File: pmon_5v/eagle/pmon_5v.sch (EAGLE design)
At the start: 33 parts, among them J1 USB, J2 USB, J3 USB_A, J4 PINHD-2X3, Q1 16Mhz, U1 LTC2943, U2 FT232RL, U3 ATMEGA328TQFP32, U4 TC1015

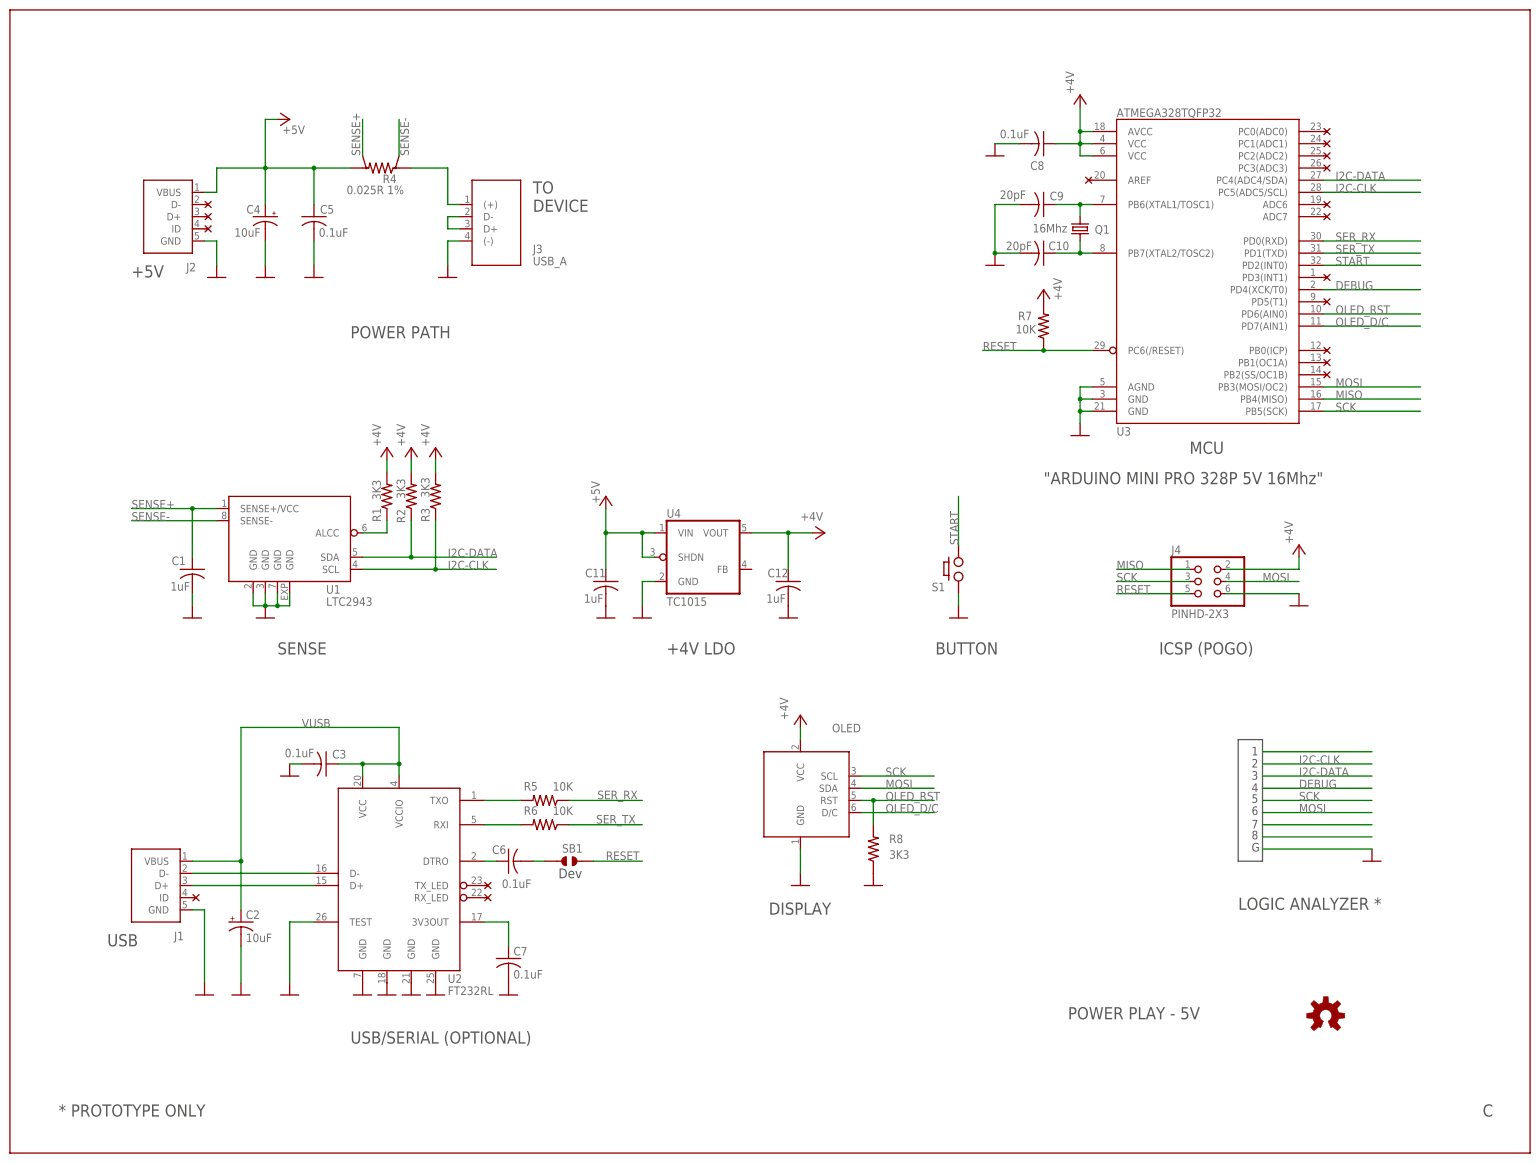
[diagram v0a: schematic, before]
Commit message: Renamed +4V network to VCC. No semantic change.
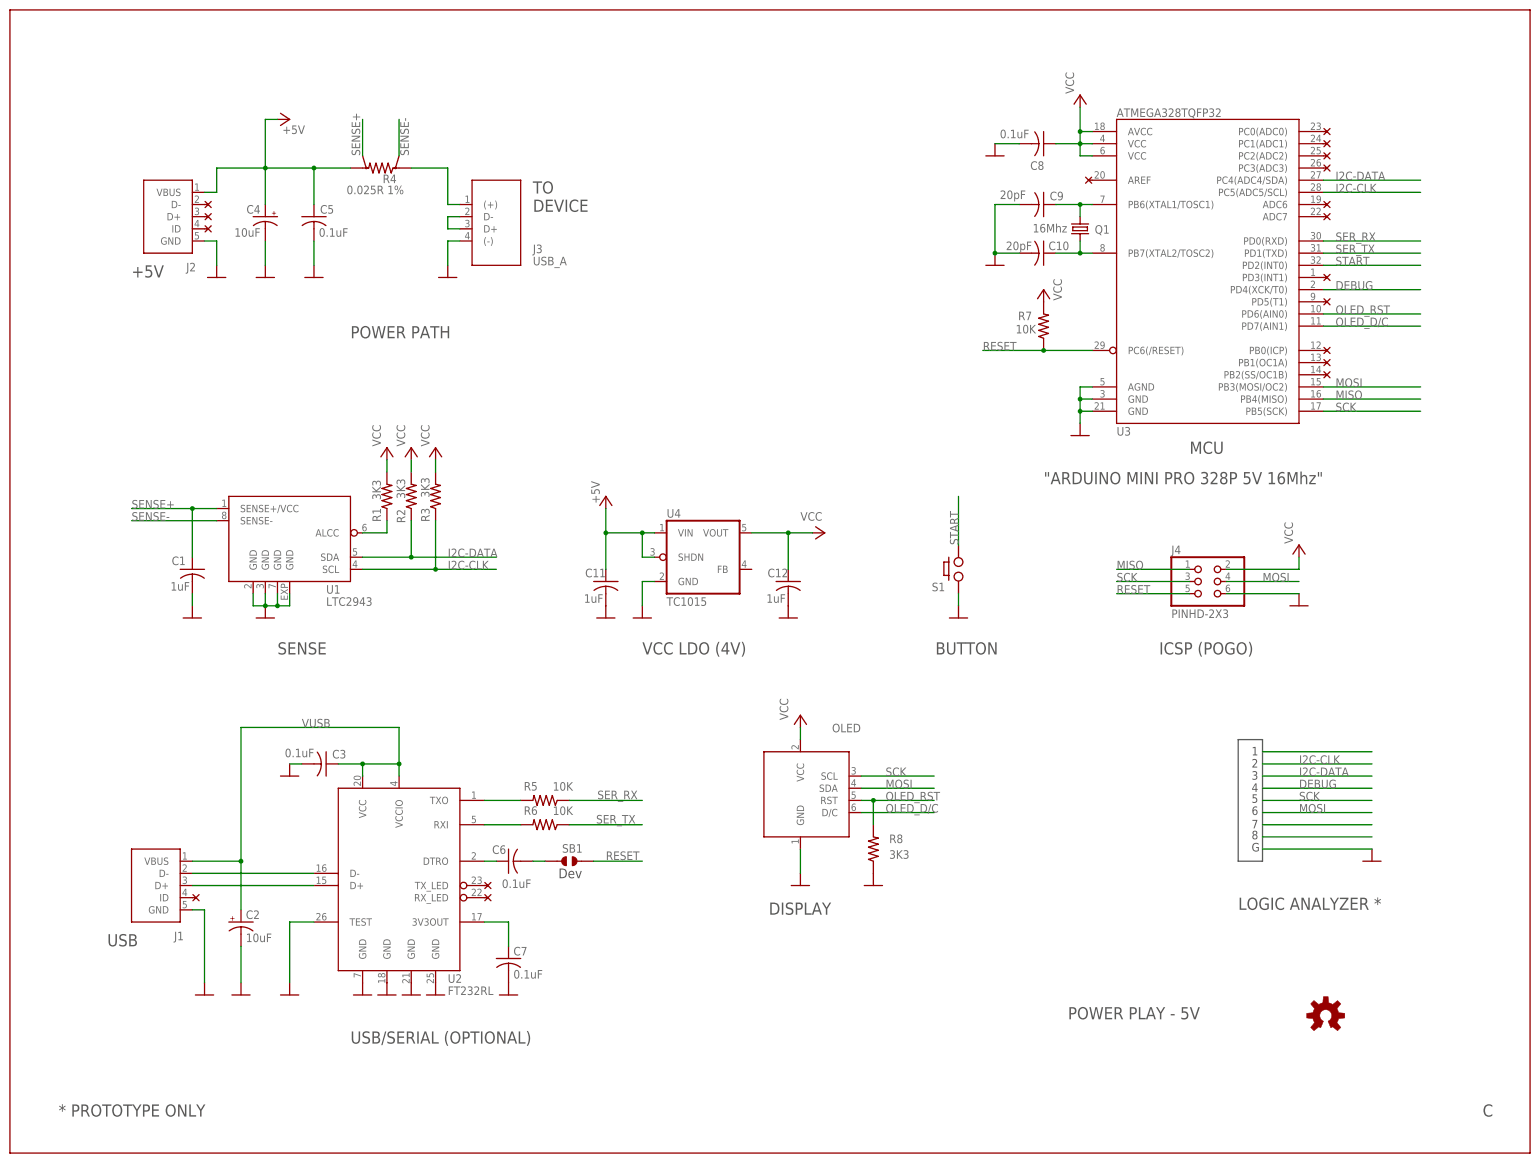
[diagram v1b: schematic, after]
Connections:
- net +4V renamed VCC
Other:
- note added: "VCC LDO (4V)"
- note removed: "+4V LDO"
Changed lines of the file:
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@@
 <part name="GND2" library="pmon_5v" deviceset="GND" device=""/>
 <part name="U4" library="pmon_5v" deviceset="TC1015" device=""/>
-<part name="U$1" library="pmon_5v" deviceset="+4V" device=""/>
+<part name="U$1" library="pmon_5v" deviceset="VCC" device=""/>
 <part name="C11" library="pmon_5v" deviceset="CAP-" device="C0603" value="1uF"/>
 <part name="C12" library="pmon_5v" deviceset="CAP-" device="C0603" value="1uF"/>
@@
 <part name="GND19" library="pmon_5v" deviceset="GND" device=""/>
 <part name="P+3" library="pmon_5v" deviceset="+5V" device=""/>
-<part name="U$15" library="pmon_5v" deviceset="+4V" device=""/>
-<part name="U$22" library="pmon_5v" deviceset="+4V" device=""/>
-<part name="U$23" library="pmon_5v" deviceset="+4V" device=""/>
-<part name="U$24" library="pmon_5v" deviceset="+4V" device=""/>
-<part name="U$25" library="pmon_5v" deviceset="+4V" device=""/>
-<part name="U$26" library="pmon_5v" deviceset="+4V" device=""/>
-<part name="U$27" library="pmon_5v" deviceset="+4V" device=""/>
+<part name="U$15" library="pmon_5v" deviceset="VCC" device=""/>
+<part name="U$22" library="pmon_5v" deviceset="VCC" device=""/>
+<part name="U$23" library="pmon_5v" deviceset="VCC" device=""/>
+<part name="U$24" library="pmon_5v" deviceset="VCC" device=""/>
+<part name="U$25" library="pmon_5v" deviceset="VCC" device=""/>
+<part name="U$26" library="pmon_5v" deviceset="VCC" device=""/>
+<part name="U$27" library="pmon_5v" deviceset="VCC" device=""/>
 <part name="U$28" library="pmon_5v" deviceset="OSH" device=""/>
 </parts>
@@
 <text x="78.994" y="57.404" size="2.032" layer="97">Dev</text>
 <text x="272.034" y="7.62" size="2.54" layer="97">C</text>
-<text x="101.6" y="104.14" size="2.54" layer="97">+4V LDO</text>
+<text x="96.52" y="104.14" size="2.54" layer="97">VCC LDO (4V)</text>
 </plain>
 <instances>
@@
 </segment>
 </net>
-<net name="+4V" class="0">
+<net name="VCC" class="0">
 <segment>
 <pinref part="R1" gate="G$1" pin="2"/>
 <wire x1="43.18" y1="144.78" x2="43.18" y2="142.24" width="0.1524" layer="91"/>
-<pinref part="U$15" gate="G$1" pin="+4V"/>
+<pinref part="U$15" gate="G$1" pin="VCC"/>
 </segment>
 <segment>
 <pinref part="R2" gate="G$1" pin="2"/>
 <wire x1="48.26" y1="144.78" x2="48.26" y2="142.24" width="0.1524" layer="91"/>
-<pinref part="U$22" gate="G$1" pin="+4V"/>
+<pinref part="U$22" gate="G$1" pin="VCC"/>
 </segment>
 <segment>
 <pinref part="R3" gate="G$1" pin="2"/>
 <wire x1="53.34" y1="144.78" x2="53.34" y2="142.24" width="0.1524" layer="91"/>
-<pinref part="U$23" gate="G$1" pin="+4V"/>
+<pinref part="U$23" gate="G$1" pin="VCC"/>
 </segment>
 <segment>
@@
 <pinref part="U3" gate="G$1" pin="VCC@1"/>
 <pinref part="U3" gate="G$1" pin="VCC@2"/>
-<pinref part="U$24" gate="G$1" pin="+4V"/>
+<pinref part="U$24" gate="G$1" pin="VCC"/>
 </segment>
 <segment>
 <pinref part="R7" gate="G$1" pin="2"/>
-<pinref part="U$25" gate="G$1" pin="+4V"/>
+<pinref part="U$25" gate="G$1" pin="VCC"/>
 </segment>
 <segment>
 <pinref part="OLED" gate="G$1" pin="VCC"/>
 <wire x1="129.54" y1="86.36" x2="129.54" y2="88.9" width="0.1524" layer="91"/>
-<pinref part="U$26" gate="G$1" pin="+4V"/>
+<pinref part="U$26" gate="G$1" pin="VCC"/>
 </segment>
 <segment>
@@
 <wire x1="218.44" y1="121.92" x2="233.68" y2="121.92" width="0.1524" layer="91"/>
 <wire x1="233.68" y1="121.92" x2="233.68" y2="124.46" width="0.1524" layer="91"/>
-<pinref part="U$27" gate="G$1" pin="+4V"/>
+<pinref part="U$27" gate="G$1" pin="VCC"/>
 </segment>
 <segment>
@@
 <wire x1="119.38" y1="129.54" x2="127" y2="129.54" width="0.1524" layer="91"/>
 <wire x1="127" y1="129.54" x2="127" y2="121.92" width="0.1524" layer="91"/>
-<pinref part="U$1" gate="G$1" pin="+4V"/>
+<pinref part="U$1" gate="G$1" pin="VCC"/>
 <wire x1="127" y1="129.54" x2="132.08" y2="129.54" width="0.1524" layer="91"/>
 <junction x="127" y="129.54"/>
